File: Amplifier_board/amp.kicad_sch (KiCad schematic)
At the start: 38 parts, among them J11 Conn_01x03_Pin, J15 Conn_01x03_Pin, U4 TPA3111D1PWPR

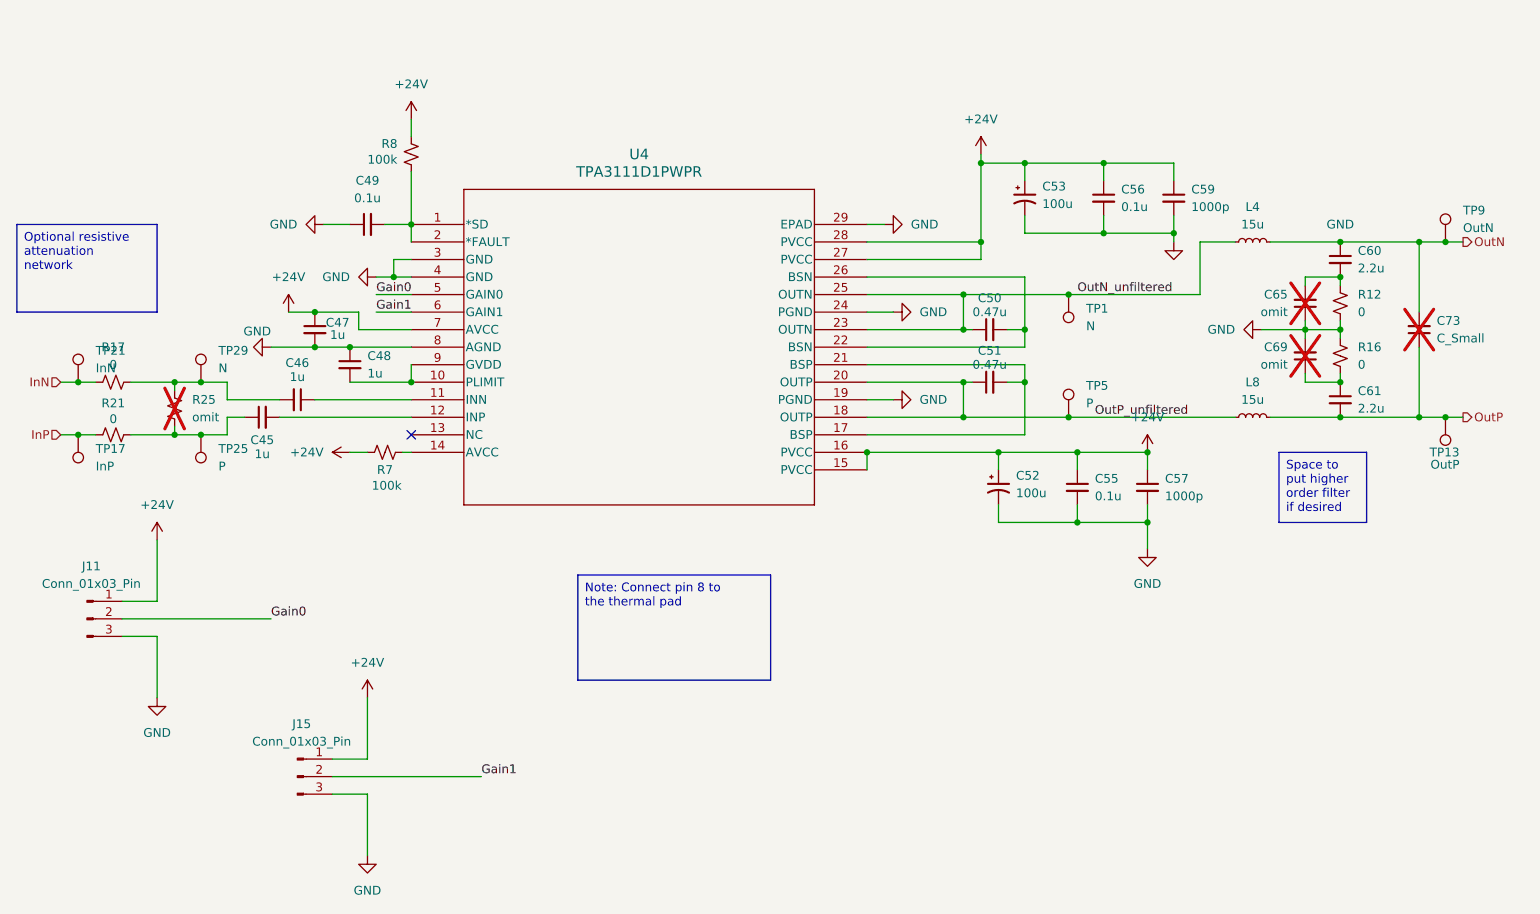
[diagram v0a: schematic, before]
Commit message: Schematic almost done on DAC board
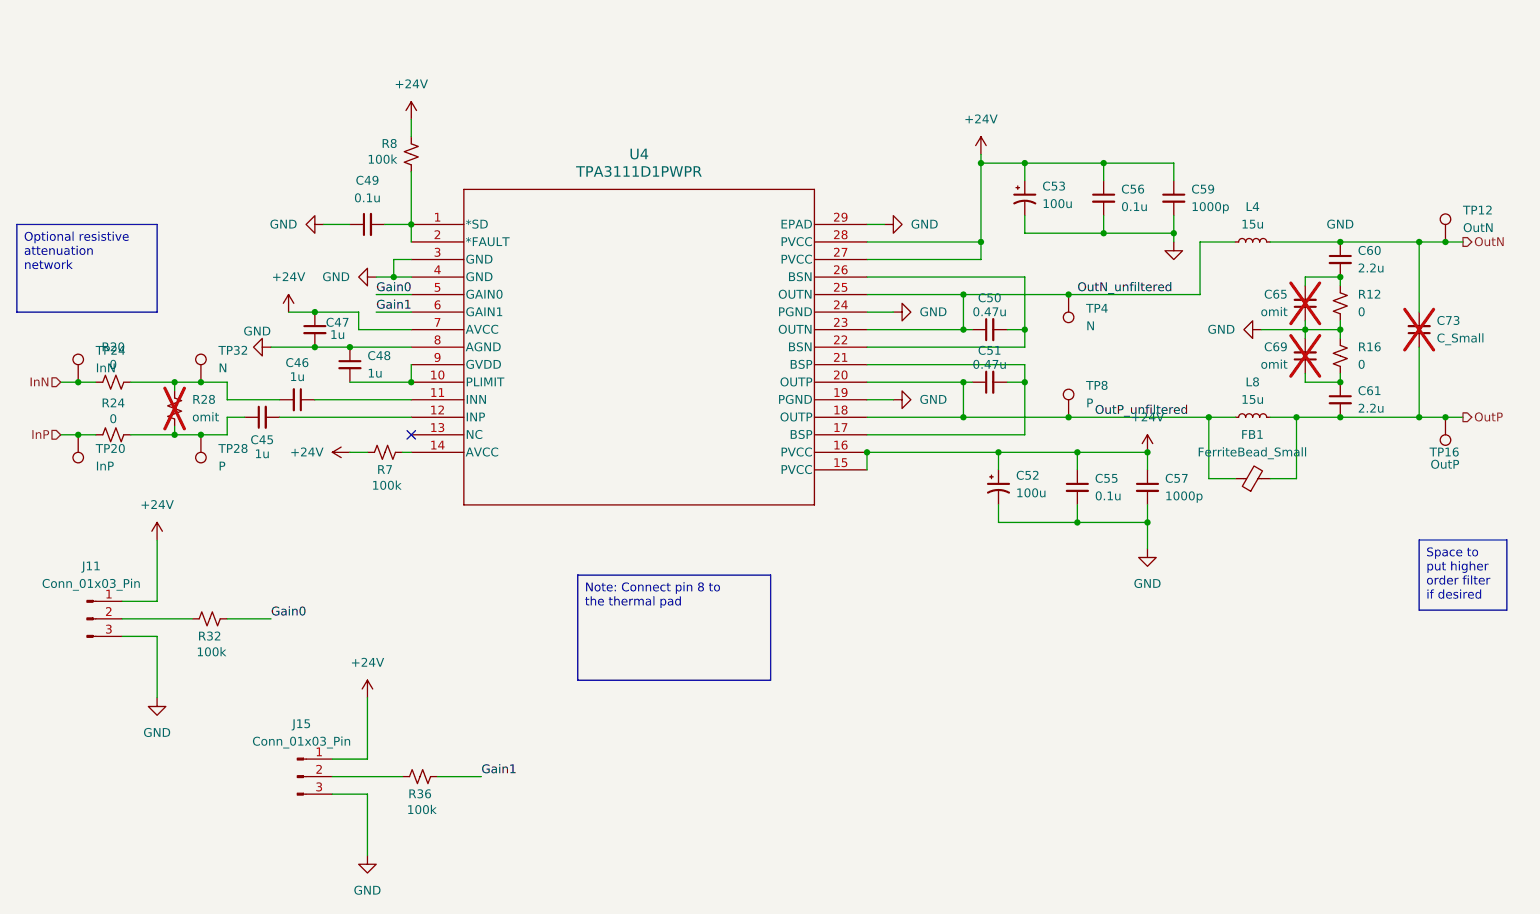
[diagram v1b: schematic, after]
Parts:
- added FB1: FerriteBead_Small, symbol Device:FerriteBead_Small
- added R32, R36: 100k, Resistor_SMD:R_0805_2012Metric_Pad1.20x1.40mm_HandSolder, symbol Device:R_Small_US
- renumbered R17 to R20, R21 to R24, R25 to R28, TP9 to TP12, TP13 to TP16, TP17 to TP20, TP21 to TP24, TP25 to TP28, TP29 to TP32, TP1 to TP4, TP5 to TP8
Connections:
- net Gain0: now also R32.2; no longer J11.2 (Pin_2)
- net Gain1: now also R36.2; no longer J15.2 (Pin_2)
- net OutP: now also FB1.2
- net OutP_unfiltered: now also FB1.1
- new net: J15.2 (Pin_2), R36.1
- new net: J11.2 (Pin_2), R32.1

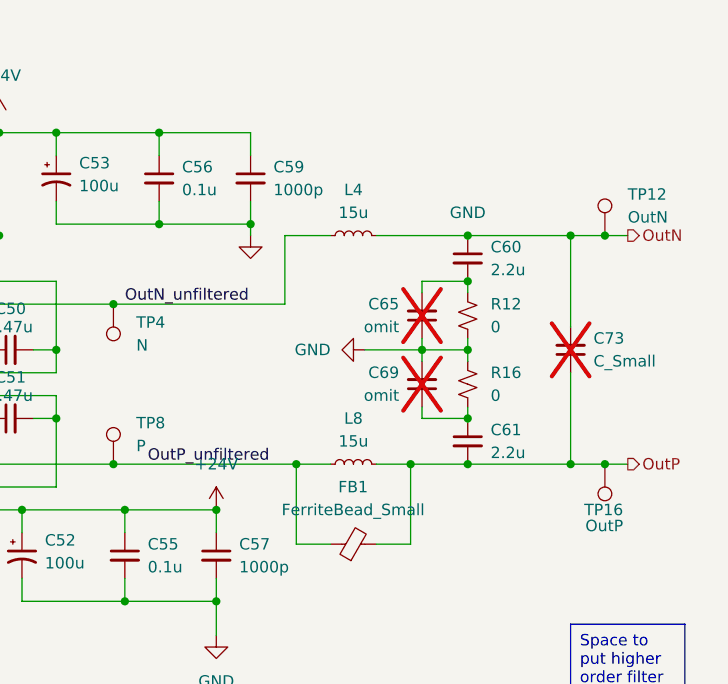
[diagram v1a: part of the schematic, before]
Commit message: Added ferrites to amp board
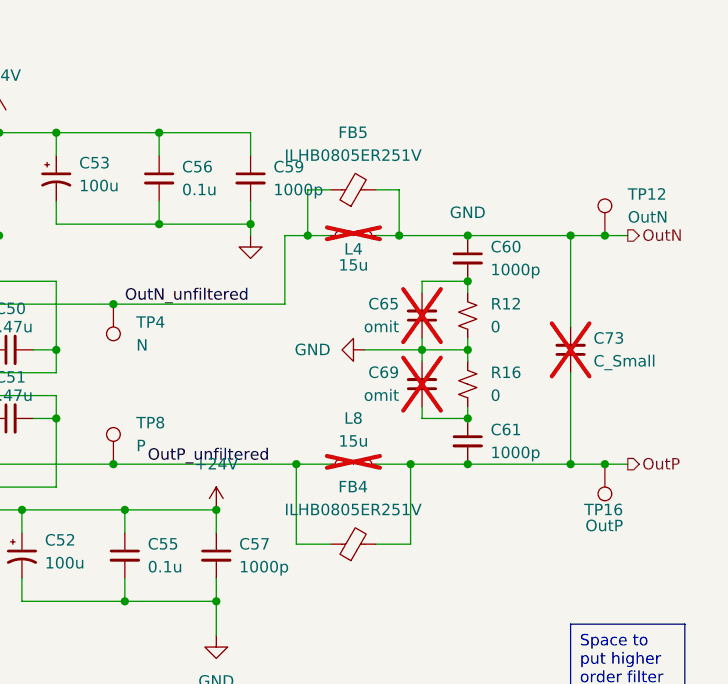
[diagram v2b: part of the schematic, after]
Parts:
- added FB5: ILHB0805ER251V, Inductor_SMD:L_0805_2012Metric_Pad1.15x1.40mm_HandSolder, symbol Device:FerriteBead_Small
- C60, C61: value 2.2u -> 1000p
- FB4: renamed from FB1; value FerriteBead_Small -> ILHB0805ER251V; footprint (none) -> Inductor_SMD:L_0805_2012Metric_Pad1.15x1.40mm_HandSolder
- L4, L8: now not fitted
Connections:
- net OutN: now also FB5.2
- net OutN_unfiltered: now also FB5.1
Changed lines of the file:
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@@
 	)
 	(junction
+		(at 229.87 66.04)
+		(diameter 0)
+		(color 0 0 0 0)
+	)
+	(junction
 		(at 248.92 66.04)
 		(diameter 0)
@@
 	)
 	(junction
+		(at 219.71 66.04)
+		(diameter 0)
+		(color 0 0 0 0)
+	)
+	(junction
 		(at 191.77 78.74)
 		(diameter 0)
@@
 	(wire
 		(pts
+			(xy 229.87 66.04) (xy 237.49 66.04)
+		)
+		(stroke
+			(width 0)
+			(type default)
+		)
+	)
+	(wire
+		(pts
 			(xy 189.23 86.36) (xy 191.77 86.36)
 		)
@@
 	(wire
 		(pts
+			(xy 219.71 66.04) (xy 222.25 66.04)
+		)
+		(stroke
+			(width 0)
+			(type default)
+		)
+	)
+	(wire
+		(pts
 			(xy 252.73 66.04) (xy 255.27 66.04)
 		)
@@
 	(wire
 		(pts
+			(xy 219.71 60.96) (xy 222.25 60.96)
+		)
+		(stroke
+			(width 0)
+			(type default)
+		)
+	)
+	(wire
+		(pts
 			(xy 96.52 132.08) (xy 96.52 140.97)
 		)
@@
 	(wire
 		(pts
+			(xy 227.33 60.96) (xy 229.87 60.96)
+		)
+		(stroke
+			(width 0)
+			(type default)
+		)
+	)
+	(wire
+		(pts
 			(xy 248.92 66.04) (xy 248.92 76.2)
 		)
@@
 	(wire
 		(pts
+			(xy 219.71 66.04) (xy 219.71 60.96)
+		)
+		(stroke
+			(width 0)
+			(type default)
+		)
+	)
+	(wire
+		(pts
 			(xy 101.6 96.52) (xy 102.87 96.52)
 		)
@@
 	(wire
 		(pts
+			(xy 229.87 60.96) (xy 229.87 66.04)
+		)
+		(stroke
+			(width 0)
+			(type default)
+		)
+	)
+	(wire
+		(pts
 			(xy 76.2 86.36) (xy 72.39 86.36)
 		)
@@
 	(wire
 		(pts
-			(xy 217.17 66.04) (xy 222.25 66.04)
+			(xy 217.17 66.04) (xy 219.71 66.04)
 		)
 		(stroke
@@
 	(wire
 		(pts
-			(xy 227.33 66.04) (xy 237.49 66.04)
+			(xy 227.33 66.04) (xy 229.87 66.04)
 		)
 		(stroke
@@
 		(in_bom yes)
 		(on_board yes)
-		(dnp no)
+		(dnp yes)
 		(fields_autoplaced yes)
 		(property "Reference" "L8"
@@
 		(in_bom yes)
 		(on_board yes)
-		(dnp no)
-		(fields_autoplaced yes)
+		(dnp yes)
 		(property "Reference" "L4"
-			(at 224.79 60.96 90)
+			(at 224.79 67.564 90)
 			(effects
 				(font
@@
 		)
 		(property "Value" "15u"
-			(at 224.79 63.5 90)
+			(at 224.79 69.342 90)
 			(effects
 				(font
@@
 		(dnp no)
 		(fields_autoplaced yes)
-		(property "Reference" "FB1"
+		(property "Reference" "FB4"
 			(at 224.7519 93.98 90)
 			(effects
@@
 			)
 		)
-		(property "Value" "FerriteBead_Small"
+		(property "Value" "ILHB0805ER251V"
 			(at 224.7519 96.52 90)
 			(effects
@@
 			)
 		)
-		(property "Footprint" ""
+		(property "Footprint" "Inductor_SMD:L_0805_2012Metric_Pad1.15x1.40mm_HandSolder"
 			(at 224.79 102.108 90)
 			(effects
@@
 	)
 	(symbol
+		(lib_id "Device:FerriteBead_Small")
+		(at 224.79 60.96 90)
+		(unit 1)
+		(exclude_from_sim no)
+		(in_bom yes)
+		(on_board yes)
+		(dnp no)
+		(fields_autoplaced yes)
+		(property "Reference" "FB5"
+			(at 224.7519 54.61 90)
+			(effects
+				(font
+					(size 1.27 1.27)
+				)
+			)
+		)
+		(property "Value" "ILHB0805ER251V"
+			(at 224.7519 57.15 90)
+			(effects
+				(font
+					(size 1.27 1.27)
+				)
+			)
+		)
+		(property "Footprint" "Inductor_SMD:L_0805_2012Metric_Pad1.15x1.40mm_HandSolder"
+			(at 224.79 62.738 90)
+			(effects
+				(font
+					(size 1.27 1.27)
+				)
+				(hide yes)
+			)
+		)
+		(property "Datasheet" "~"
+			(at 224.79 60.96 0)
+			(effects
+				(font
+					(size 1.27 1.27)
+				)
+				(hide yes)
+			)
+		)
+		(property "Description" "Ferrite bead, small symbol"
+			(at 224.79 60.96 0)
+			(effects
+				(font
+					(size 1.27 1.27)
+				)
+				(hide yes)
+			)
+		)
+		(pin "2"
+		)
+		(pin "1"
+		)
+		(instances
+			(project "Amplifier_board"
+				(path "/991395a4-3885-4774-b551-0bfe029123d3/1a21d9eb-2329-48b7-8877-ba841ad5b065"
+					(reference "FB8")
+					(unit 1)
+				)
+				(path "/991395a4-3885-4774-b551-0bfe029123d3/26541e86-2f42-461f-bb67-92277cc28a80"
+					(reference "FB5")
+					(unit 1)
+				)
+				(path "/991395a4-3885-4774-b551-0bfe029123d3/e8898fe0-55dc-4973-83e9-f265cc01a132"
+					(reference "FB7")
+					(unit 1)
+				)
+				(path "/991395a4-3885-4774-b551-0bfe029123d3/eadc8ba5-6d36-4b46-a20f-2896249de991"
+					(reference "FB6")
+					(unit 1)
+				)
+			)
+		)
+	)
+	(symbol
 		(lib_id "Connector:TestPoint")
 		(at 252.73 66.04 0)
@@
 			)
 		)
-		(property "Value" "2.2u"
+		(property "Value" "1000p"
 			(at 240.03 69.8562 0)
 			(effects
@@
 			)
 		)
-		(property "Value" "2.2u"
+		(property "Value" "1000p"
 			(at 240.03 90.1762 0)
 			(effects
